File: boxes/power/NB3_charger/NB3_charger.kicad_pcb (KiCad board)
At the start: 2 copper layers, 65 x 150.1 mm, 58 parts, among them J1 Barrel_Jack-DC-5.5-2.1, J2 B4B-PH-K-S, J3 Conn_01x02_Pin, J4 Conn_01x02_Pin, J5 Conn_01x02_Pin, J6 Conn_01x02_Pin, Q1 PMOS_FDC658AP, SW1 SW_SPDT, SW2 SW_SPDT, T1 NTCG163JF103FT1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

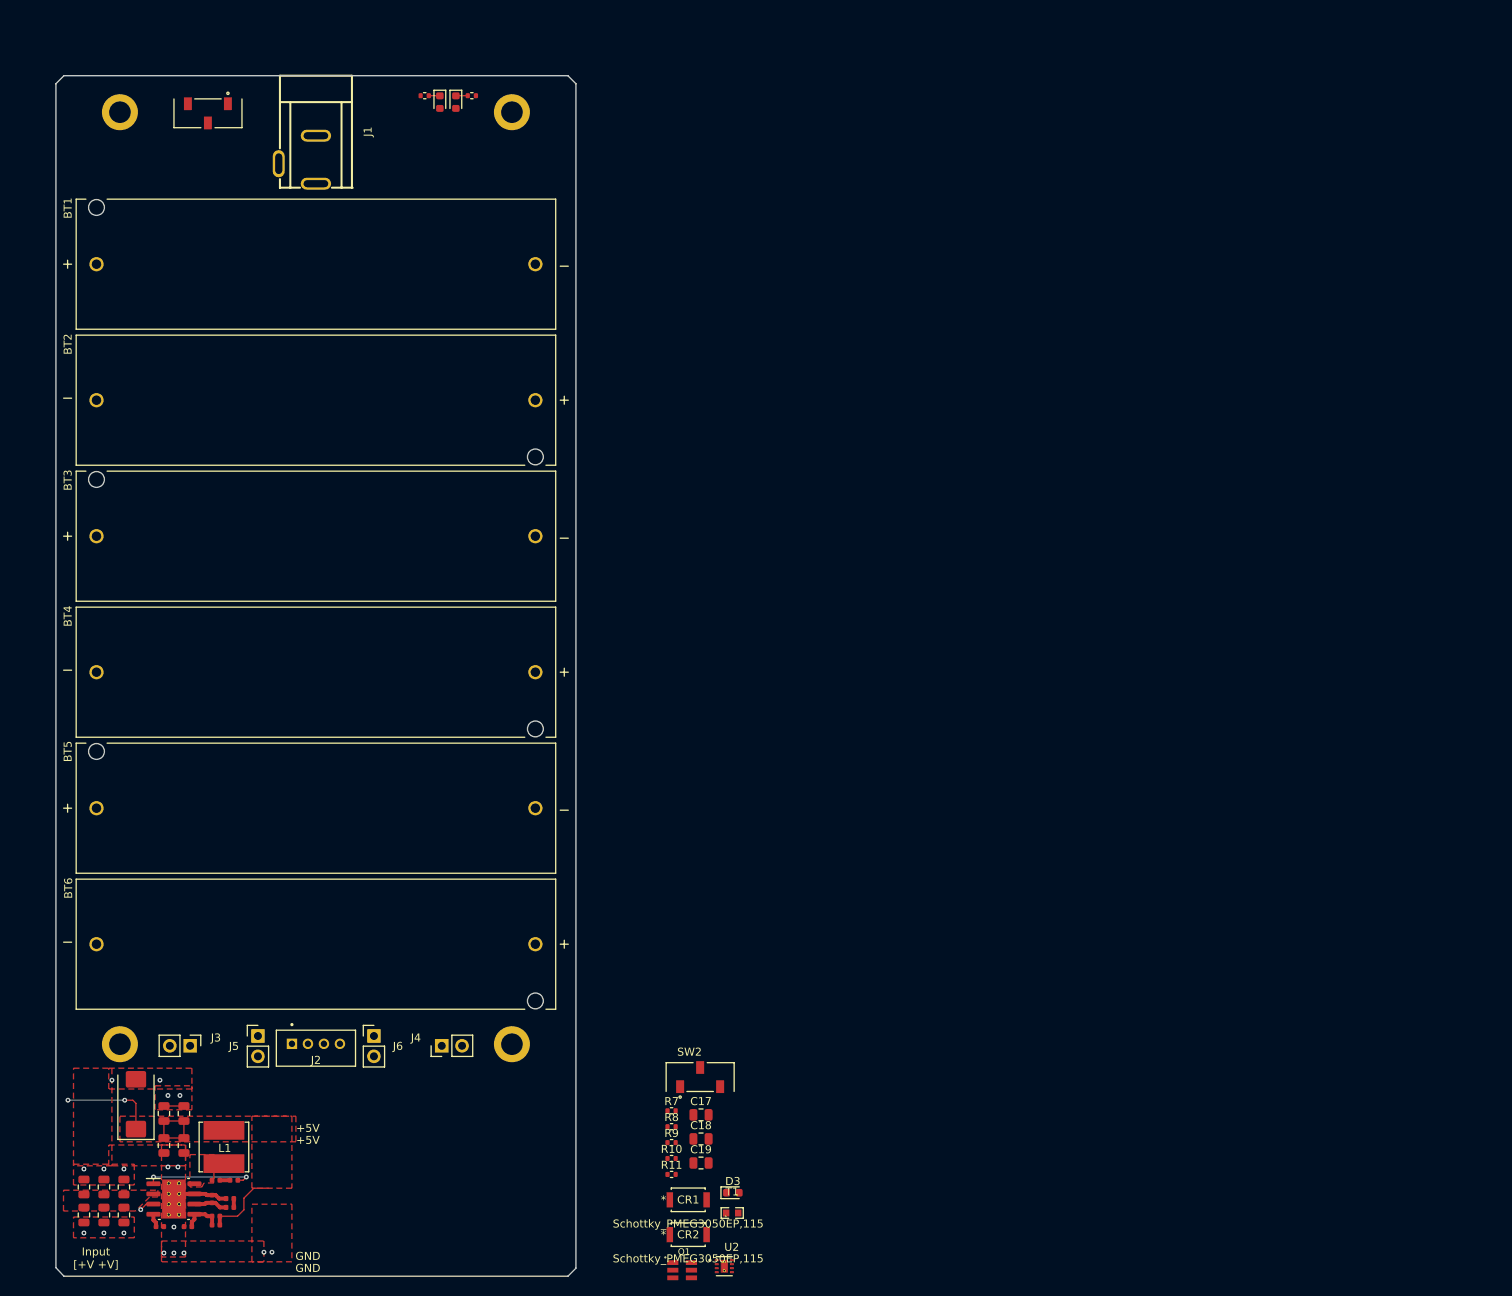
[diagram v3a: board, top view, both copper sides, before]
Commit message: Update NB3 Charger (schematic notes)
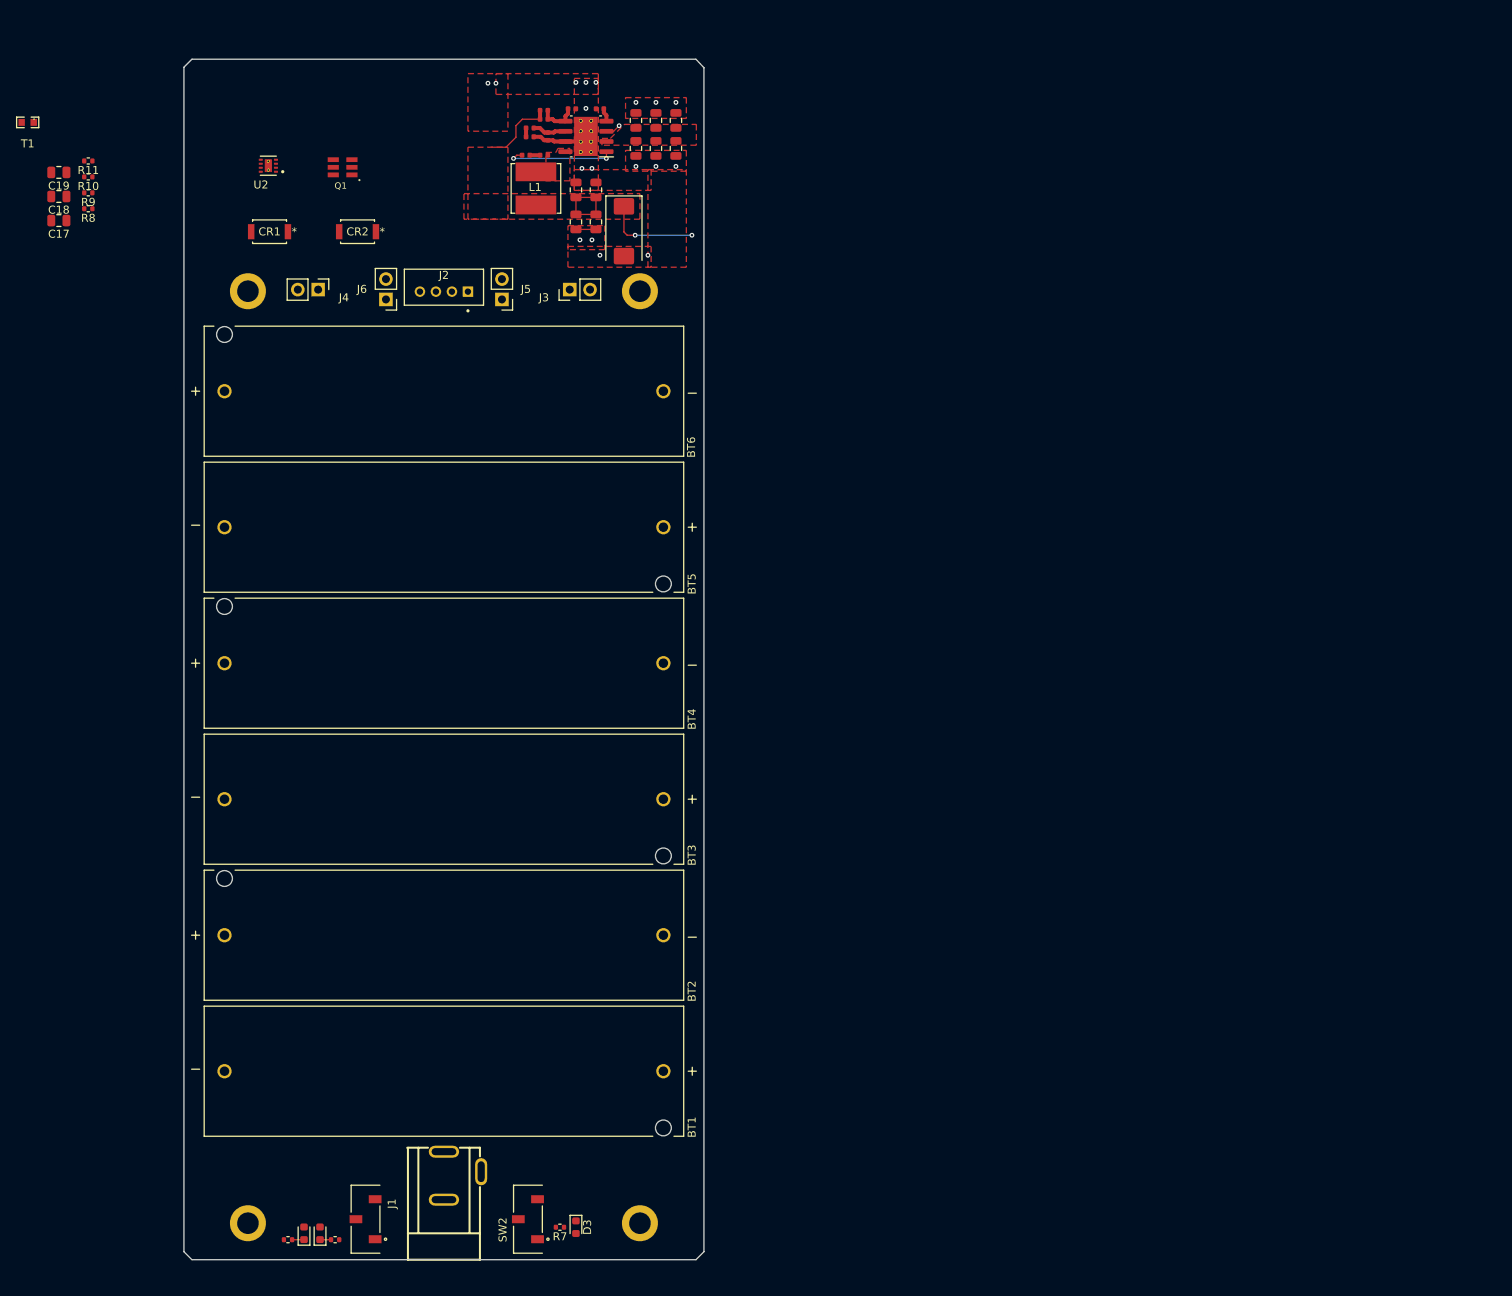
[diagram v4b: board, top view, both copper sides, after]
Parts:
- D3: value LED (Green) -> LED (Yellow)
- moved T1 162.3 mm to (56.5, 33.5), turned to 180 degrees
- moved C3 155.6 mm to (137.5, 33.3), turned to 90 degrees
- moved H1 153.3 mm to (133.0, 171.1), turned to 180 degrees
- moved C1 153.2 mm to (135.0, 33.3), turned to 90 degrees
- moved C2 151.1 mm to (132.5, 33.3), turned to 90 degrees
- moved C8 150.2 mm to (128.0, 31.8), turned to 180 degrees
- moved C4 149.4 mm to (137.5, 36.8), turned to -90 degrees
- moved U2 148.9 mm to (86.6, 38.9), turned to 180 degrees
- moved R5 147.7 mm to (124.5, 31.8), turned to 0 degrees
- moved C19 147.6 mm to (60.4, 39.8), turned to 180 degrees
- moved C5 147.0 mm to (135.0, 36.8), turned to -90 degrees
- moved R11 146.2 mm to (64.0, 38.3), turned to 180 degrees
- moved C11 145.2 mm to (121.0, 32.0), turned to 0 degrees
- moved R6 144.8 mm to (89.0, 173.2), turned to 180 degrees
- moved C6 144.7 mm to (132.5, 36.8), turned to -90 degrees
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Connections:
- J5 pad 2: +12V -> VDC
- J6 pad 2: +12V -> VDC
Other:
- outline, holes or cut-outs redrawn
- board text removed: "+5V"
- board text removed: "GND"
- board text removed: "Input [+V +V]"
